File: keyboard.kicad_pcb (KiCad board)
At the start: 2 copper layers, 361 x 94.6 mm, 159 parts, among them IC1 ATMEGA32U4, J1 MINI, X1 ASX3F

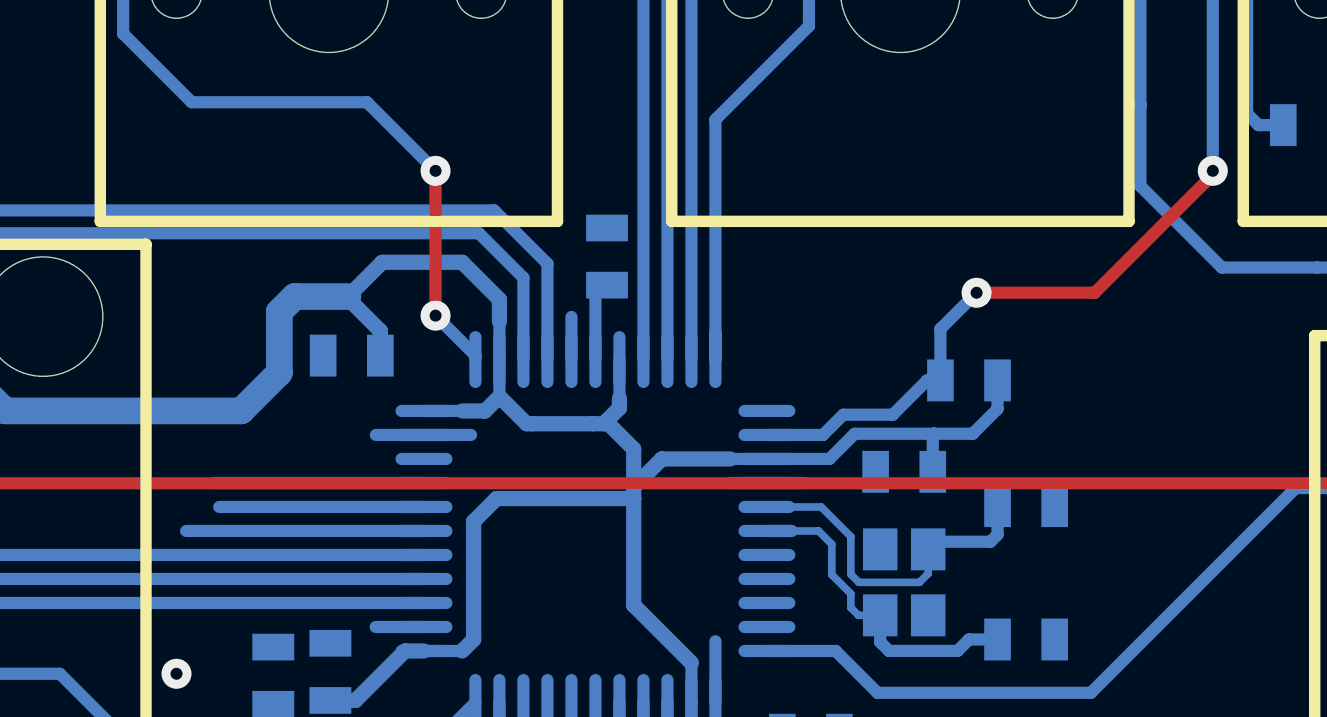
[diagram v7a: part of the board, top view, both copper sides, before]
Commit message: Connect col6
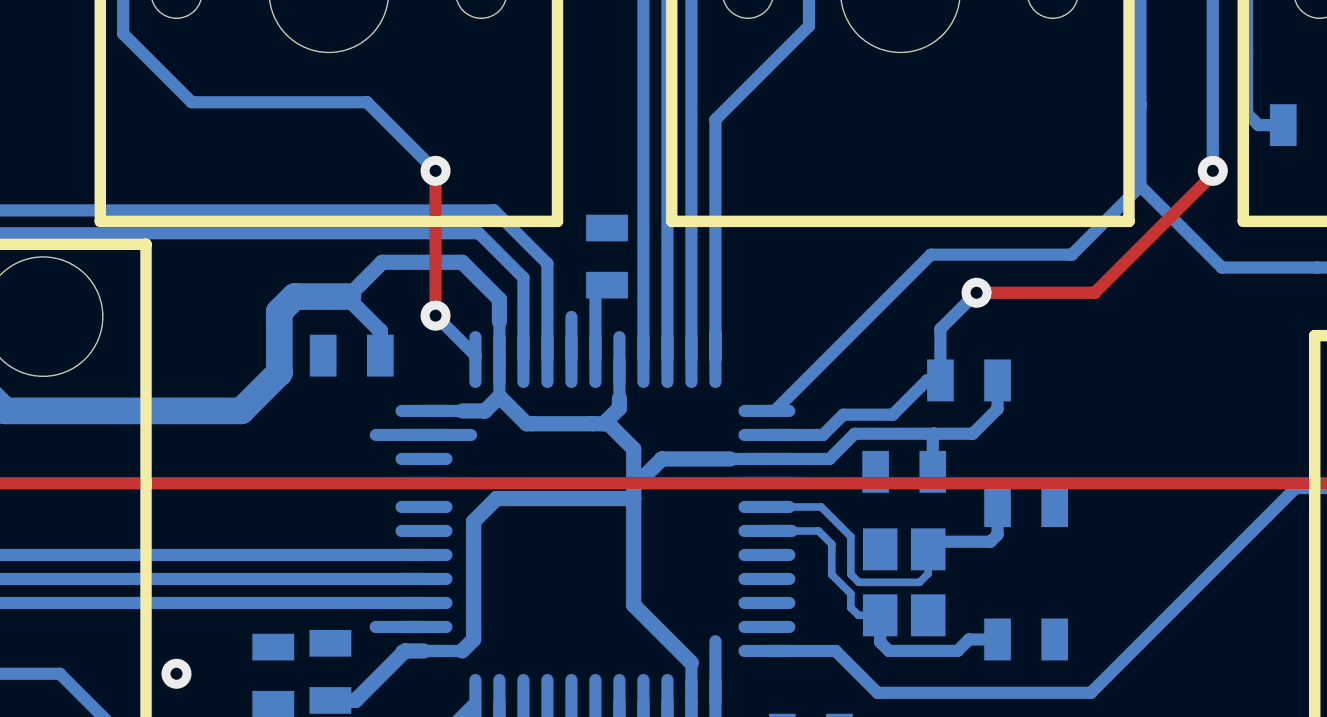
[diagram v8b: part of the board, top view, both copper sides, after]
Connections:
- IC1 pad 12: Net-(IC1-Pad12) -> /col6
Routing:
- net /col6: track 94.8 -> 110.3 mm
- net Net-(IC1-Pad39): track 7.93 -> 0.00 mm
- net Net-(IC1-Pad41): track 6.97 -> 0.00 mm
- net Net-(IC1-Pad40): track 6.82 -> 0.00 mm
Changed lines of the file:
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@@
     (thickness 1.6002)
     (drawings 325)
-    (tracks 1215)
+    (tracks 1216)
     (zones 0)
     (modules 159)
-    (nets 113)
+    (nets 112)
   )
   (page A2)
@@
   (net 99 "Net-(IC1-Pad41)")
   (net 100 "Net-(IC1-Pad13)")
-  (net 101 "Net-(IC1-Pad12)")
-  (net 102 "Net-(IC1-Pad18)")
-  (net 103 "Net-(IC1-Pad19)")
-  (net 104 "Net-(IC1-Pad20)")
-  (net 105 "Net-(IC1-Pad21)")
-  (net 106 "Net-(IC1-Pad28)")
-  (net 107 "Net-(IC1-Pad27)")
-  (net 108 "Net-(IC1-Pad26)")
-  (net 109 "Net-(IC1-Pad25)")
-  (net 110 "Net-(IC1-Pad29)")
-  (net 111 "Net-(IC1-Pad30)")
-  (net 112 "Net-(IC1-Pad31)")
+  (net 101 "Net-(IC1-Pad18)")
+  (net 102 "Net-(IC1-Pad19)")
+  (net 103 "Net-(IC1-Pad20)")
+  (net 104 "Net-(IC1-Pad21)")
+  (net 105 "Net-(IC1-Pad28)")
+  (net 106 "Net-(IC1-Pad27)")
+  (net 107 "Net-(IC1-Pad26)")
+  (net 108 "Net-(IC1-Pad25)")
+  (net 109 "Net-(IC1-Pad29)")
+  (net 110 "Net-(IC1-Pad30)")
+  (net 111 "Net-(IC1-Pad31)")
   (net_class Default "This is the default net class."
     (clearance 0.2032)
@@
     (add_net "Net-(D70-Pad2)")
     (add_net "Net-(D71-Pad2)")
-    (add_net "Net-(IC1-Pad12)")
     (add_net "Net-(IC1-Pad13)")
     (add_net "Net-(IC1-Pad18)")
@@
       (net 100 "Net-(IC1-Pad13)"))
     (pad 12 smd oval (at -4.0005 -5.715 270) (size 0.4064 1.89992) (layers B.Cu B.Paste B.Mask)
-      (net 101 "Net-(IC1-Pad12)"))
+      (net 33 /col6))
     (pad 18 smd oval (at 0.8001 -5.715 270) (size 0.4064 1.89992) (layers B.Cu B.Paste B.Mask)
-      (net 102 "Net-(IC1-Pad18)"))
+      (net 101 "Net-(IC1-Pad18)"))
     (pad 19 smd oval (at 1.6002 -5.715 270) (size 0.4064 1.89992) (layers B.Cu B.Paste B.Mask)
-      (net 103 "Net-(IC1-Pad19)"))
+      (net 102 "Net-(IC1-Pad19)"))
     (pad 20 smd oval (at 2.4003 -5.715 270) (size 0.4064 1.89992) (layers B.Cu B.Paste B.Mask)
-      (net 104 "Net-(IC1-Pad20)"))
+      (net 103 "Net-(IC1-Pad20)"))
     (pad 21 smd oval (at 3.2004 -5.715 270) (size 0.4064 1.89992) (layers B.Cu B.Paste B.Mask)
-      (net 105 "Net-(IC1-Pad21)"))
+      (net 104 "Net-(IC1-Pad21)"))
     (pad 22 smd oval (at 4.0005 -5.715 270) (size 0.4064 1.89992) (layers B.Cu B.Paste B.Mask)
       (net 83 /row5))
@@
       (net 5 "Net-(C3-Pad1)"))
     (pad 28 smd oval (at 5.715 0 270) (size 1.89992 0.4064) (layers B.Cu B.Paste B.Mask)
-      (net 106 "Net-(IC1-Pad28)"))
+      (net 105 "Net-(IC1-Pad28)"))
     (pad 7 smd oval (at -5.715 -0.8001 270) (size 1.89992 0.4064) (layers B.Cu B.Paste B.Mask)
       (net 2 VCC))
     (pad 27 smd oval (at 5.715 -0.8001 270) (size 1.89992 0.4064) (layers B.Cu B.Paste B.Mask)
-      (net 107 "Net-(IC1-Pad27)"))
+      (net 106 "Net-(IC1-Pad27)"))
     (pad 26 smd oval (at 5.715 -1.6002 270) (size 1.89992 0.4064) (layers B.Cu B.Paste B.Mask)
-      (net 108 "Net-(IC1-Pad26)"))
+      (net 107 "Net-(IC1-Pad26)"))
     (pad 8 smd oval (at -5.715 -1.6002 270) (size 1.89992 0.4064) (layers B.Cu B.Paste B.Mask)
       (net 79 /row1))
@@
       (net 80 /row2))
     (pad 25 smd oval (at 5.715 -2.4003 270) (size 1.89992 0.4064) (layers B.Cu B.Paste B.Mask)
-      (net 109 "Net-(IC1-Pad25)"))
+      (net 108 "Net-(IC1-Pad25)"))
     (pad 24 smd oval (at 5.715 -3.2004 270) (size 1.89992 0.4064) (layers B.Cu B.Paste B.Mask)
       (net 2 VCC))
@@
       (net 1 GND))
     (pad 29 smd oval (at 5.715 0.8001 270) (size 1.89992 0.4064) (layers B.Cu B.Paste B.Mask)
-      (net 110 "Net-(IC1-Pad29)"))
+      (net 109 "Net-(IC1-Pad29)"))
     (pad 5 smd oval (at -5.715 0.8001 270) (size 1.89992 0.4064) (layers B.Cu B.Paste B.Mask)
       (net 1 GND))
@@
       (net 84 "Net-(IC1-Pad4)"))
     (pad 30 smd oval (at 5.715 1.6002 270) (size 1.89992 0.4064) (layers B.Cu B.Paste B.Mask)
-      (net 111 "Net-(IC1-Pad30)"))
+      (net 110 "Net-(IC1-Pad30)"))
     (pad 31 smd oval (at 5.715 2.4003 270) (size 1.89992 0.4064) (layers B.Cu B.Paste B.Mask)
-      (net 112 "Net-(IC1-Pad31)"))
+      (net 111 "Net-(IC1-Pad31)"))
     (pad 3 smd oval (at -5.715 2.4003 270) (size 1.89992 0.4064) (layers B.Cu B.Paste B.Mask)
       (net 85 "Net-(IC1-Pad3)"))
@@
   (segment (start 179.451 123.571) (end 179.451 134.6835) (width 0.4064) (layer B.Cu) (net 33))
   (segment (start 174.4345 116.332) (end 174.4345 117.7925) (width 0.4064) (layer B.Cu) (net 33))
+  (segment (start 166.99992 144.90954) (end 167.25646 144.90954) (width 0.4064) (layer B.Cu) (net 33))
+  (segment (start 167.25646 144.90954) (end 172.466 139.7) (width 0.4064) (layer B.Cu) (net 33))
+  (segment (start 177.165 139.7) (end 179.451 137.414) (width 0.4064) (layer B.Cu) (net 33))
+  (segment (start 172.466 139.7) (end 177.165 139.7) (width 0.4064) (layer B.Cu) (net 33))
   (segment (start 169.799 69.31152) (end 169.2275 68.74002) (width 0.4064) (layer B.Cu) (net 34))
   (segment (start 164.338 76.454) (end 164.846 76.962) (width 0.4064) (layer B.Cu) (net 34))
@@
   (segment (start 262.509 143.637) (end 263.779 144.907) (width 0.4064) (layer B.Cu) (net 94))
   (segment (start 260.858 143.637) (end 262.509 143.637) (width 0.4064) (layer B.Cu) (net 94))
-  (segment (start 155.56992 148.91004) (end 147.64004 148.91004) (width 0.4064) (layer B.Cu) (net 97))
-  (segment (start 155.56992 148.10994) (end 148.74494 148.10994) (width 0.4064) (layer B.Cu) (net 98))
-  (segment (start 155.56992 147.30984) (end 148.60016 147.30984) (width 0.4064) (layer B.Cu) (net 99))
   (segment (start 172.339 143.891) (end 172.7835 143.891) (width 0.4064) (layer B.Cu) (net 100))
-  (segment (start 162.08502 154.62504) (end 162.08502 156.49702) (width 0.4064) (layer B.Cu) (net 107))
-  (segment (start 162.08502 156.49702) (end 164.084 158.496) (width 0.4064) (layer B.Cu) (net 107))
-  (segment (start 164.084 158.496) (end 170.18 158.496) (width 0.4064) (layer B.Cu) (net 107))
-  (segment (start 162.88512 154.62504) (end 162.88512 156.28112) (width 0.4064) (layer B.Cu) (net 108))
-  (segment (start 162.88512 156.28112) (end 164.338 157.734) (width 0.4064) (layer B.Cu) (net 108))
-  (segment (start 164.338 157.734) (end 170.18 157.734) (width 0.4064) (layer B.Cu) (net 108))
-  (segment (start 163.68522 154.62504) (end 163.68522 156.06522) (width 0.4064) (layer B.Cu) (net 109))
-  (segment (start 163.68522 156.06522) (end 164.592 156.972) (width 0.4064) (layer B.Cu) (net 109))
-  (segment (start 164.592 156.972) (end 170.18 156.972) (width 0.4064) (layer B.Cu) (net 109))
+  (segment (start 162.08502 154.62504) (end 162.08502 156.49702) (width 0.4064) (layer B.Cu) (net 106))
+  (segment (start 162.08502 156.49702) (end 164.084 158.496) (width 0.4064) (layer B.Cu) (net 106))
+  (segment (start 164.084 158.496) (end 170.18 158.496) (width 0.4064) (layer B.Cu) (net 106))
+  (segment (start 162.88512 154.62504) (end 162.88512 156.28112) (width 0.4064) (layer B.Cu) (net 107))
+  (segment (start 162.88512 156.28112) (end 164.338 157.734) (width 0.4064) (layer B.Cu) (net 107))
+  (segment (start 164.338 157.734) (end 170.18 157.734) (width 0.4064) (layer B.Cu) (net 107))
+  (segment (start 163.68522 154.62504) (end 163.68522 156.06522) (width 0.4064) (layer B.Cu) (net 108))
+  (segment (start 163.68522 156.06522) (end 164.592 156.972) (width 0.4064) (layer B.Cu) (net 108))
+  (segment (start 164.592 156.972) (end 170.18 156.972) (width 0.4064) (layer B.Cu) (net 108))
   (zone (net 1) (net_name GND) (layer F.Cu) (hatch edge 0.508)
     (connect_pads (clearance 0.308))
